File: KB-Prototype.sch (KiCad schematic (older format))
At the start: 45 parts, among them J1 Conn_01x04, J2 Conn_01x04, J3 Conn_01x04, SW1 SW_Push, U1 ATmega32U4-AU, Y1 Resonator_Small

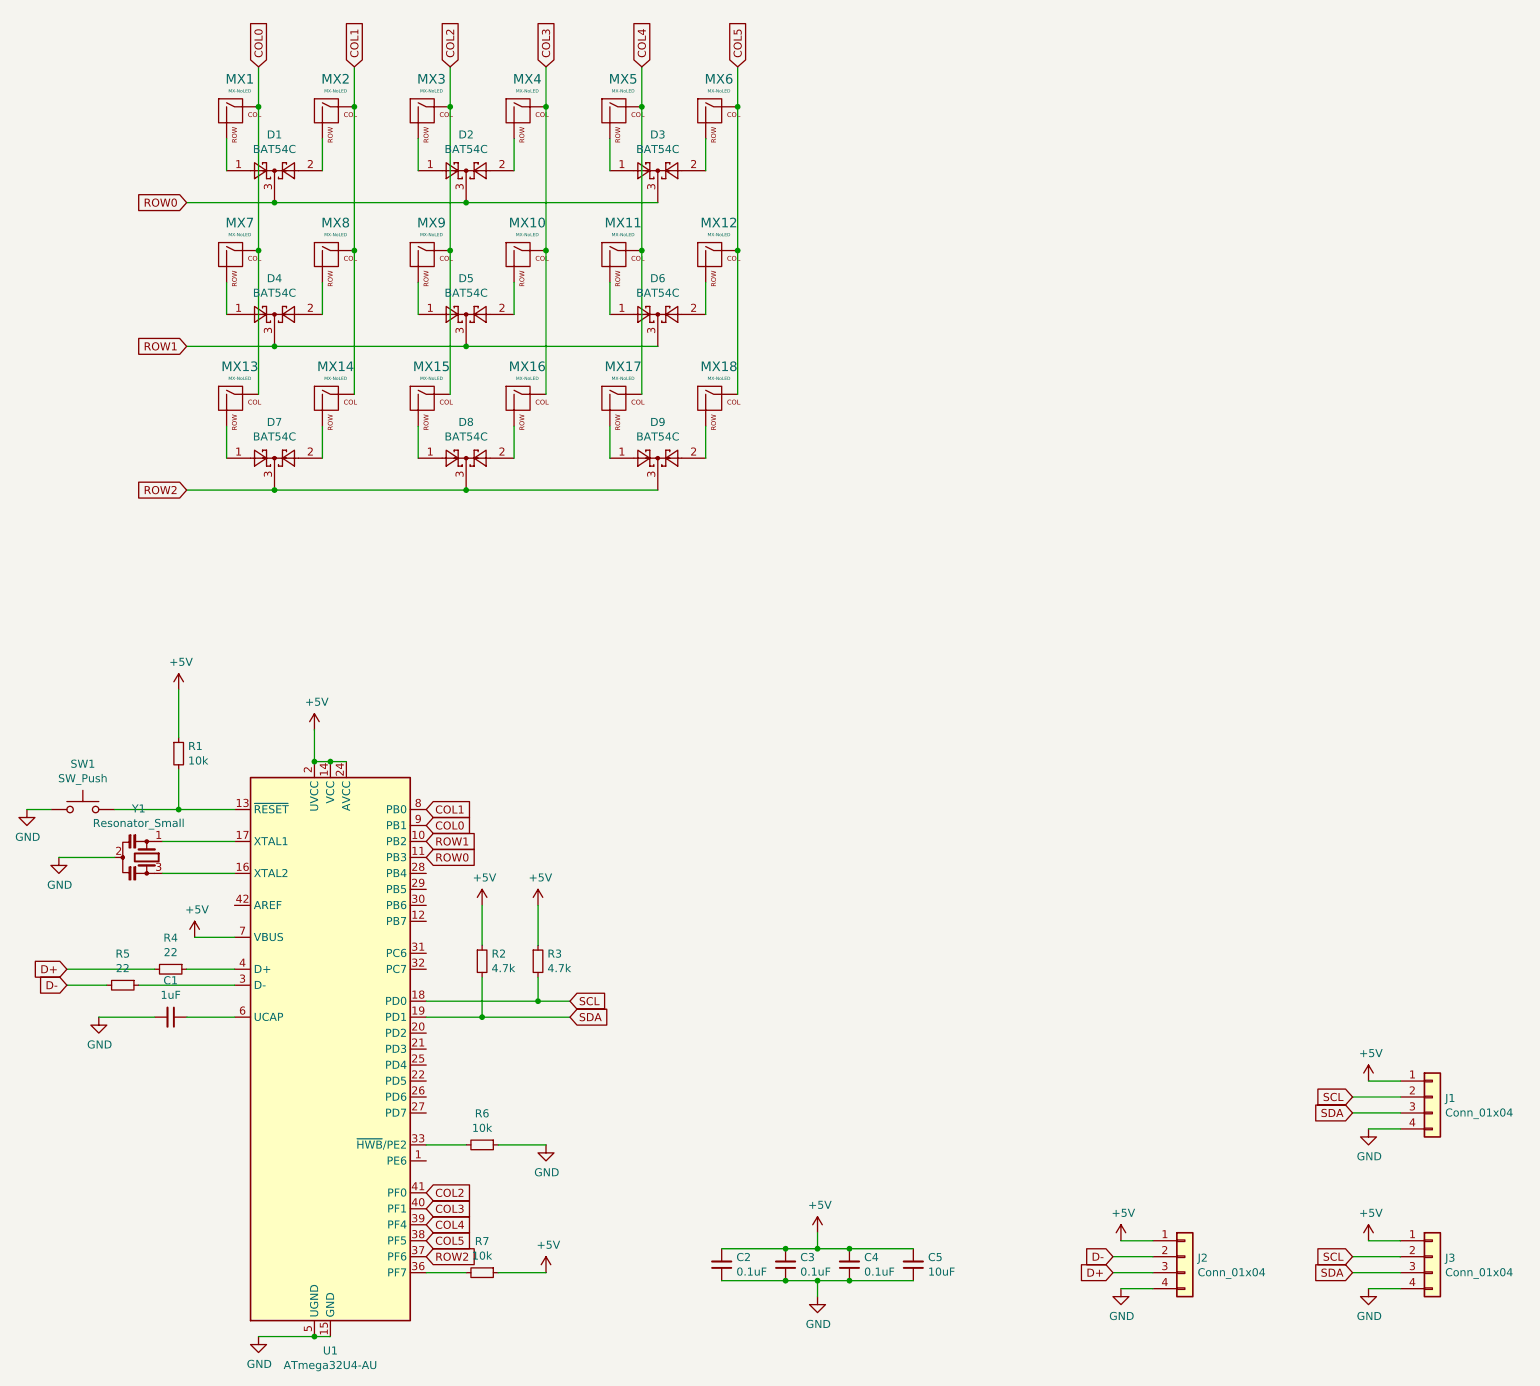
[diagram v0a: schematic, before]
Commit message: modified sch to suit right half
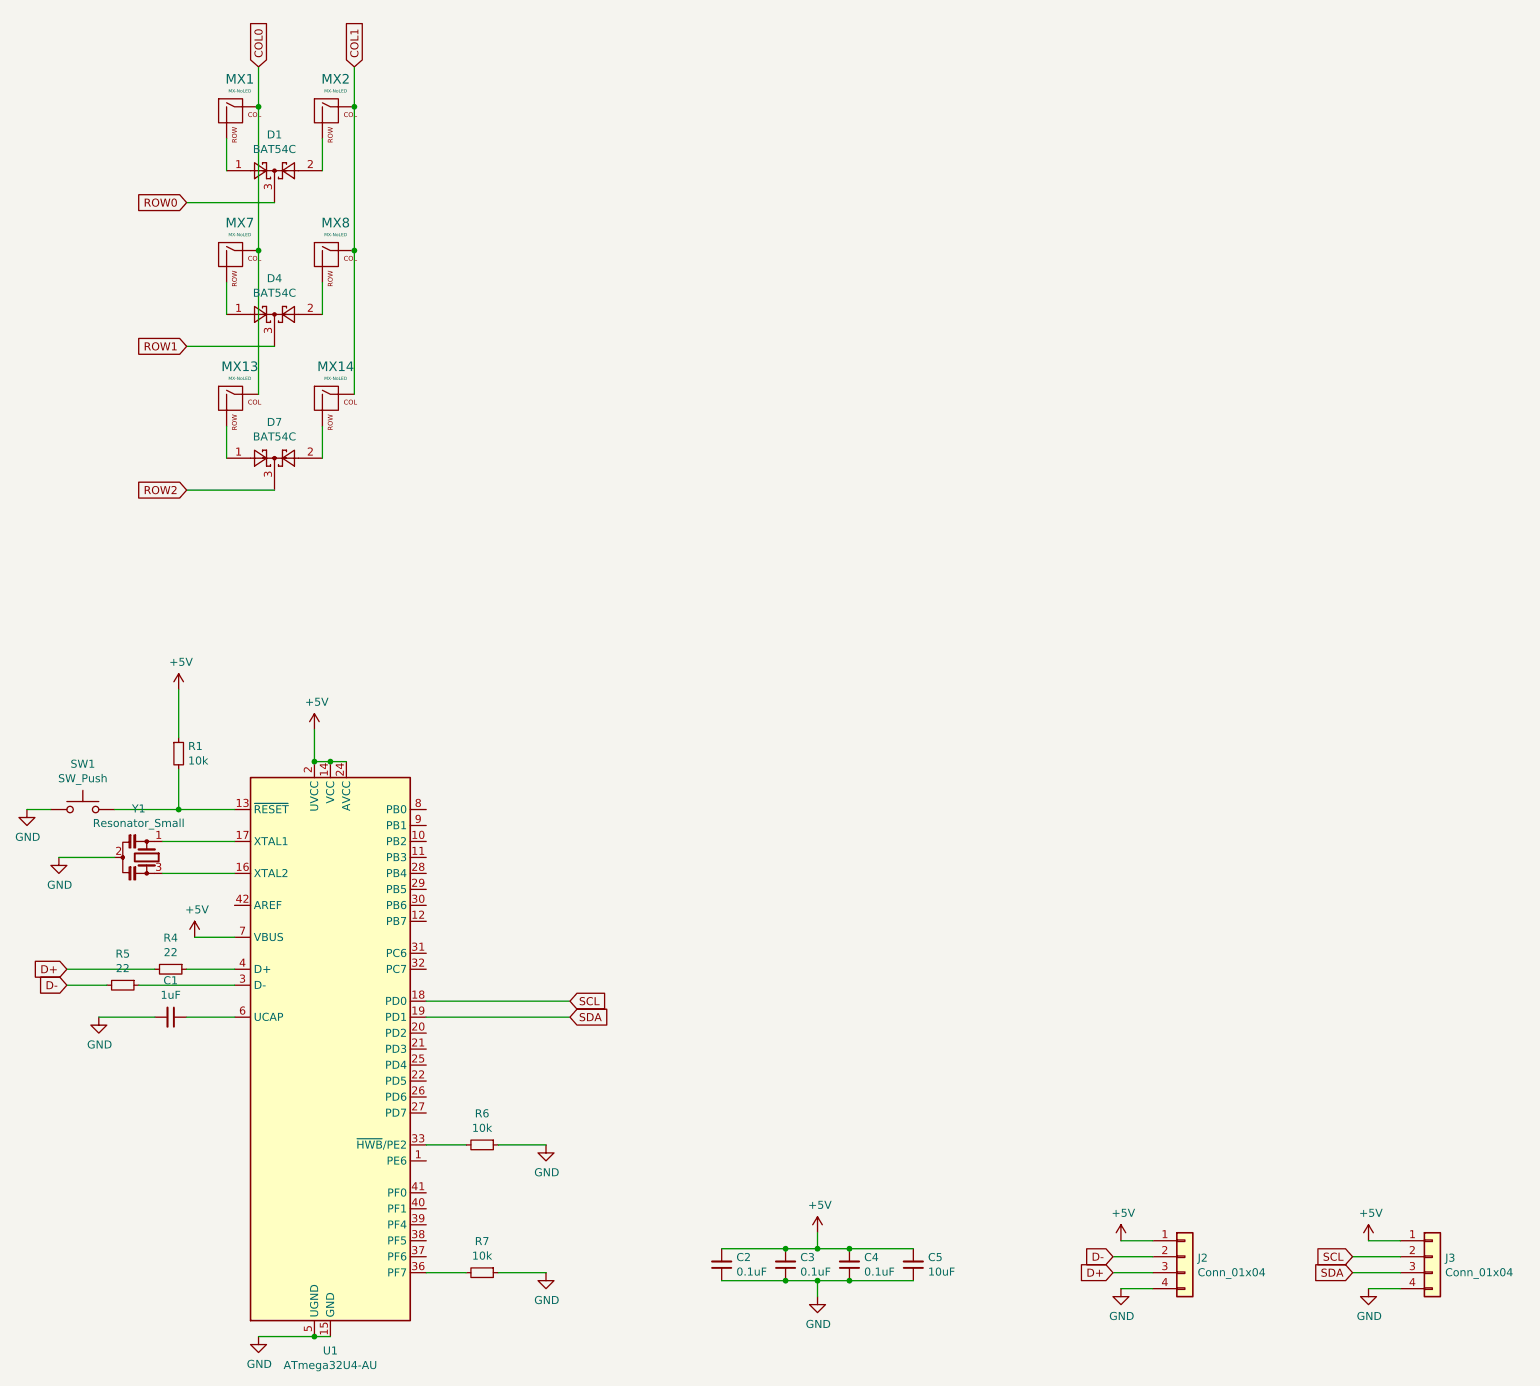
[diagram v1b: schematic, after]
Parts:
- removed D2, D3, D5, D6, D8, D9: BAT54C, Package_TO_SOT_SMD:SOT-23, symbol Diode:BAT54C
- removed J1: Conn_01x04, random-keyboard-parts:JST-SR-4, symbol Connector_Generic:Conn_01x04
- removed MX10, MX11, MX12, MX15, MX16, MX17, MX18, MX3, MX4, MX5, MX6, MX9: MX-NoLED, MX_Only:MXOnly-1U-NoLED, symbol MX_Alps_Hybrid:MX-NoLED
- removed R2, R3: 4.7k, Resistor_SMD:R_0805_2012Metric, symbol Device:R_Small
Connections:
- net +5V: no longer R7.1
- net COL0: no longer U1.9 (PB1)
- net COL1: no longer U1.8 (PB0)
- net GND: now also R7.1
- net ROW0: no longer U1.11 (PB3)
- net ROW1: no longer U1.10 (PB2)
- net ROW2: no longer U1.37 (PF6)
- net COL2: no longer names the net of U1.41 (PF0)
- net COL3: no longer names the net of U1.40 (PF1)
- net COL4: no longer names the net of U1.39 (PF4)
- net COL5: no longer names the net of U1.38 (PF5)

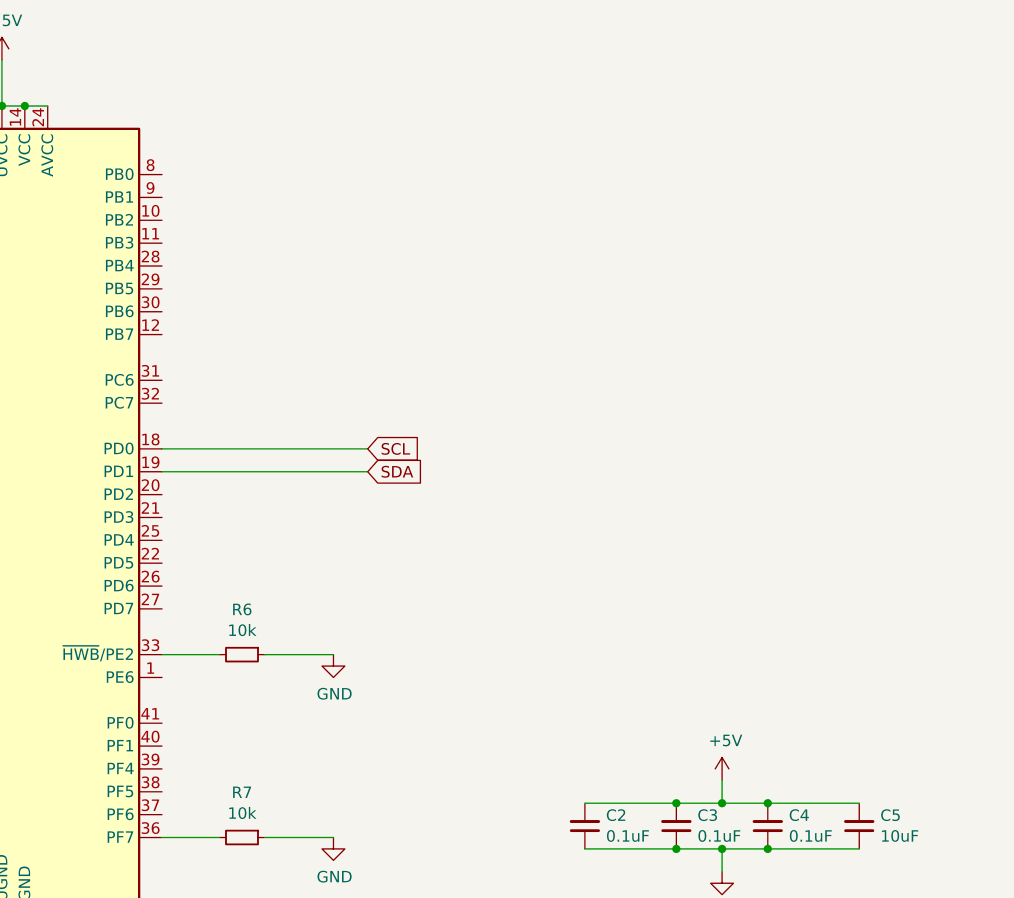
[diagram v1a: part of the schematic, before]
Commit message: traced right half, added mounting holes
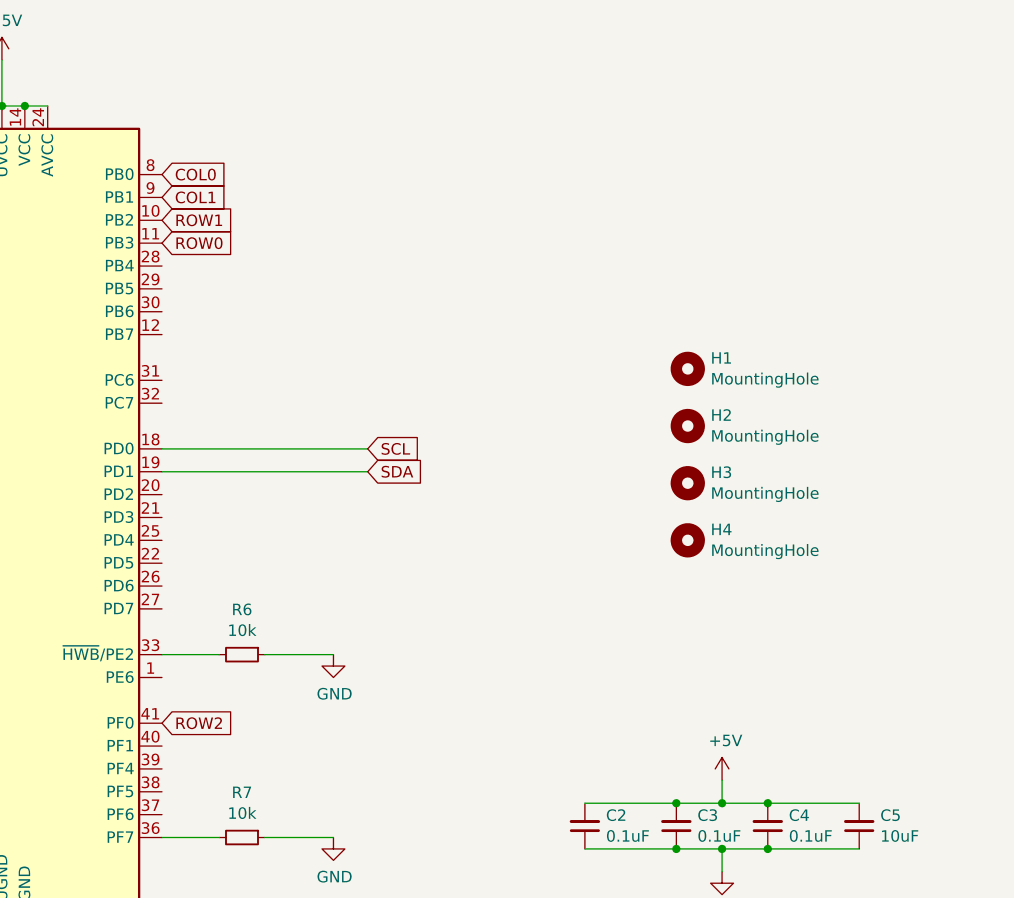
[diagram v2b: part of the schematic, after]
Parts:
- added H1, H2, H3, H4: MountingHole, random-keyboard-parts:Generic-Mounthole, symbol Mechanical:MountingHole
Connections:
- net COL0: now also U1.8 (PB0)
- net COL1: now also U1.9 (PB1)
- net ROW0: now also U1.11 (PB3)
- net ROW1: now also U1.10 (PB2)
- net ROW2: now also U1.41 (PF0)
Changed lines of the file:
@@
 Wire Wire Line
 	3350 8200 4250 8200
+Text GLabel 3350 7300 2    50   Input ~ 0
+ROW0
+Text GLabel 3350 7200 2    50   Input ~ 0
+ROW1
+Text GLabel 3350 9400 2    50   Input ~ 0
+ROW2
+Text GLabel 3350 7000 2    50   Input ~ 0
+COL0
+Text GLabel 3350 7100 2    50   Input ~ 0
+COL1
+$Comp
+L Mechanical:MountingHole H3
+U 1 1 5F0C5942
+P 5650 8350
+F 0 "H3" H 5750 8396 50  0000 L CNN
+F 1 "MountingHole" H 5750 8305 50  0000 L CNN
+F 2 "random-keyboard-parts:Generic-Mounthole" H 5650 8350 50  0001 C CNN
+F 3 "~" H 5650 8350 50  0001 C CNN
+	1    5650 8350
+	1    0    0    -1
+$EndComp
+$Comp
+L Mechanical:MountingHole H4
+U 1 1 5F0C6836
+P 5650 8600
+F 0 "H4" H 5750 8646 50  0000 L CNN
+F 1 "MountingHole" H 5750 8555 50  0000 L CNN
+F 2 "random-keyboard-parts:Generic-Mounthole" H 5650 8600 50  0001 C CNN
+F 3 "~" H 5650 8600 50  0001 C CNN
+	1    5650 8600
+	1    0    0    -1
+$EndComp
+$Comp
+L Mechanical:MountingHole H2
+U 1 1 5F0C6B0F
+P 5650 8100
+F 0 "H2" H 5750 8146 50  0000 L CNN
+F 1 "MountingHole" H 5750 8055 50  0000 L CNN
+F 2 "random-keyboard-parts:Generic-Mounthole" H 5650 8100 50  0001 C CNN
+F 3 "~" H 5650 8100 50  0001 C CNN
+	1    5650 8100
+	1    0    0    -1
+$EndComp
+$Comp
+L Mechanical:MountingHole H1
+U 1 1 5F0C724C
+P 5650 7850
+F 0 "H1" H 5750 7896 50  0000 L CNN
+F 1 "MountingHole" H 5750 7805 50  0000 L CNN
+F 2 "random-keyboard-parts:Generic-Mounthole" H 5650 7850 50  0001 C CNN
+F 3 "~" H 5650 7850 50  0001 C CNN
+	1    5650 7850
+	1    0    0    -1
+$EndComp
 $EndSCHEMATC
